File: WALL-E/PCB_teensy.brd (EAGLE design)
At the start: 92.8 x 115.8 mm, 42 parts, among them U4 R-78E5.0-0.5

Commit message: cleaned up each layer
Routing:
- net 8: track 90.0 -> 90.5 mm
- net 0/RX: track 94.4 -> 93.9 mm
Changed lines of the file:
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@@
 <contactref element="U$1" pad="0/RX"/>
 <contactref element="J1" pad="3"/>
-<wire x1="62.9" y1="29.37" x2="62.9" y2="28.85" width="0.1524" layer="1"/>
 <via x="69.5" y="30.25" extent="1-16" drill="0.35"/>
 <wire x1="74.98" y1="102.48" x2="86.75" y2="102.48" width="0.1524" layer="1"/>
@@
 <via x="69.5" y="27.75" extent="1-16" drill="0.35"/>
 <wire x1="50.2" y1="29.37" x2="52.8075" y2="26.7625" width="0.1524" layer="1"/>
-<wire x1="52.8075" y1="26.7625" x2="52.8075" y2="25.80045625" width="0.1524" layer="1"/>
-<wire x1="52.8075" y1="25.80045625" x2="53.85795625" y2="24.75" width="0.1524" layer="1"/>
-<wire x1="53.85795625" y1="24.75" x2="59.5" y2="24.75" width="0.1524" layer="1"/>
-<wire x1="59.5" y1="24.75" x2="62.4452" y2="27.6952" width="0.1524" layer="1"/>
-<wire x1="69.4452" y1="27.6952" x2="69.5" y2="27.75" width="0.1524" layer="1"/>
-<wire x1="62.4452" y1="27.6952" x2="69.4452" y2="27.6952" width="0.1524" layer="1"/>
+<wire x1="52.8075" y1="25.80045625" x2="52.8075" y2="26.7625" width="0.1524" layer="1"/>
+<wire x1="59.5" y1="25" x2="62.9452" y2="27.4452" width="0.1524" layer="1"/>
 <wire x1="69.5" y1="27.75" x2="73.25" y2="31.5" width="0.1524" layer="15"/>
 <wire x1="73.25" y1="31.5" x2="73.25" y2="84.25" width="0.1524" layer="15"/>
@@
 <wire x1="73.25" y1="84.25" x2="77.48" y2="88.48" width="0.1524" layer="1"/>
 <wire x1="77.48" y1="88.48" x2="86.75" y2="88.48" width="0.1524" layer="1"/>
+<wire x1="53.60795625" y1="25" x2="52.8075" y2="25.80045625" width="0.1524" layer="1"/>
+<wire x1="59.5" y1="25" x2="53.60795625" y2="25" width="0.1524" layer="1"/>
+<wire x1="69.1952" y1="27.4452" x2="69.5" y2="27.75" width="0.1524" layer="1"/>
+<wire x1="62.9452" y1="27.4452" x2="69.1952" y2="27.4452" width="0.1524" layer="1"/>
 </signal>
 <signal name="6">
@@
 <via x="68.5" y="26.5" extent="1-16" drill="0.35"/>
 <wire x1="50.25" y1="25.75" x2="51.5548" y2="24.4452" width="0.1524" layer="1"/>
-<wire x1="61.68105625" y1="26.5" x2="68.5" y2="26.5" width="0.1524" layer="1"/>
-<wire x1="59.62625625" y1="24.4452" x2="61.68105625" y2="26.5" width="0.1524" layer="1"/>
+<wire x1="62.68105625" y1="26.5" x2="68.5" y2="26.5" width="0.1524" layer="1"/>
+<wire x1="59.62625625" y1="24.4452" x2="62.68105625" y2="26.5" width="0.1524" layer="1"/>
 <wire x1="51.5548" y1="24.4452" x2="59.62625625" y2="24.4452" width="0.1524" layer="1"/>
 <wire x1="68.5" y1="26.5" x2="69.75" y2="26.5" width="0.1524" layer="15"/>
@@
 <wire x1="45.12" y1="29.37" x2="47.5" y2="26.99" width="0.1524" layer="1"/>
 <wire x1="47.5" y1="26.99" x2="47.5" y2="25.5" width="0.1524" layer="1"/>
-<wire x1="47.5" y1="25.5" x2="48.8596" y2="24.1404" width="0.1524" layer="1"/>
-<wire x1="48.8596" y1="24.1404" x2="59.7525125" y2="24.1404" width="0.1524" layer="1"/>
-<wire x1="59.7525125" y1="24.1404" x2="60.80605625" y2="25.19394375" width="0.1524" layer="1"/>
-<wire x1="60.80605625" y1="25.19394375" x2="69.44394375" y2="25.19394375" width="0.1524" layer="1"/>
+<wire x1="47.5" y1="25.5" x2="48.8596" y2="23.8904" width="0.1524" layer="1"/>
+<wire x1="48.8596" y1="23.8904" x2="59.7525125" y2="23.8904" width="0.1524" layer="1"/>
+<wire x1="59.7525125" y1="23.8904" x2="61.80605625" y2="25.19394375" width="0.1524" layer="1"/>
+<wire x1="61.80605625" y1="25.19394375" x2="69.44394375" y2="25.19394375" width="0.1524" layer="1"/>
 <wire x1="69.44394375" y1="25.19394375" x2="69.5" y2="25.25" width="0.1524" layer="1"/>
 <via x="69.5" y="25.25" extent="1-16" drill="0.35"/>
@@
 <contactref element="J3" pad="4"/>
 <via x="68.5" y="24" extent="1-16" drill="0.35"/>
-<wire x1="59.87876875" y1="23.8356" x2="60.04316875" y2="24" width="0.1524" layer="1"/>
-<wire x1="60.04316875" y1="24" x2="68.5" y2="24" width="0.1524" layer="1"/>
-<wire x1="42.58" y1="29.37" x2="48.1144" y2="23.8356" width="0.1524" layer="1"/>
-<wire x1="48.1144" y1="23.8356" x2="59.87876875" y2="23.8356" width="0.1524" layer="1"/>
+<wire x1="48.1144" y1="23.3356" x2="42.58" y2="29.37" width="0.1524" layer="1"/>
 <wire x1="68.5" y1="24" x2="70" y2="24" width="0.1524" layer="15"/>
 <wire x1="70" y1="24" x2="76.25" y2="30.25" width="0.1524" layer="15"/>
@@
 <wire x1="76.25" y1="70.5" x2="77.69" y2="71.94" width="0.1524" layer="1"/>
 <wire x1="77.69" y1="71.94" x2="86.75" y2="71.94" width="0.1524" layer="1"/>
+<wire x1="68.5" y1="24" x2="67.8356" y2="23.3356" width="0.1524" layer="1"/>
+<wire x1="67.8356" y1="23.3356" x2="48.1144" y2="23.3356" width="0.1524" layer="1"/>
 </signal>
 <signal name="24">
@@
 <via x="66.75" y="37" extent="1-16" drill="0.35"/>
 <wire x1="66.75" y1="37" x2="76.75" y2="37" width="0.1524" layer="2"/>
-<wire x1="76.75" y1="37" x2="77" y2="37" width="0.1524" layer="2"/>
 <via x="81.75" y="26.25" extent="1-16" drill="0.35"/>
 <wire x1="81.75" y1="26.25" x2="81.77" y2="26.23" width="0.1524" layer="1"/>
@@
 <wire x1="21.53" y1="9.72" x2="21.53" y2="8.75" width="0.1524" layer="1"/>
 <wire x1="18.12" y1="13.13" x2="21.53" y2="9.72" width="0.1524" layer="1"/>
-<wire x1="21.53" y1="8.75" x2="26.03" y2="4.5" width="0.1524" layer="1"/>
-<wire x1="26.03" y1="4.5" x2="74.75" y2="4.5" width="0.1524" layer="1"/>
+<wire x1="21.53" y1="8.75" x2="25.78" y2="4.5" width="0.1524" layer="1"/>
+<wire x1="25.78" y1="4.5" x2="74.75" y2="4.5" width="0.1524" layer="1"/>
 <wire x1="74.75" y1="4.5" x2="77" y2="7" width="0.1524" layer="1"/>
 <wire x1="77" y1="7" x2="77" y2="39.5" width="0.1524" layer="1"/>
@@
 <wire x1="24.07" y1="9.68" x2="24.07" y2="8.75" width="0.1524" layer="1"/>
 <wire x1="20.62" y1="13.13" x2="24.07" y2="9.68" width="0.1524" layer="1"/>
-<wire x1="24.07" y1="8.75" x2="28.07" y2="5" width="0.1524" layer="1"/>
-<wire x1="28.07" y1="5" x2="74.25" y2="5" width="0.1524" layer="1"/>
+<wire x1="24.07" y1="8.75" x2="27.82" y2="5" width="0.1524" layer="1"/>
+<wire x1="27.82" y1="5" x2="74.25" y2="5" width="0.1524" layer="1"/>
 <wire x1="74.25" y1="5" x2="75.75" y2="6.5" width="0.1524" layer="1"/>
 <wire x1="75.75" y1="6.5" x2="75.75" y2="39.5" width="0.1524" layer="1"/>

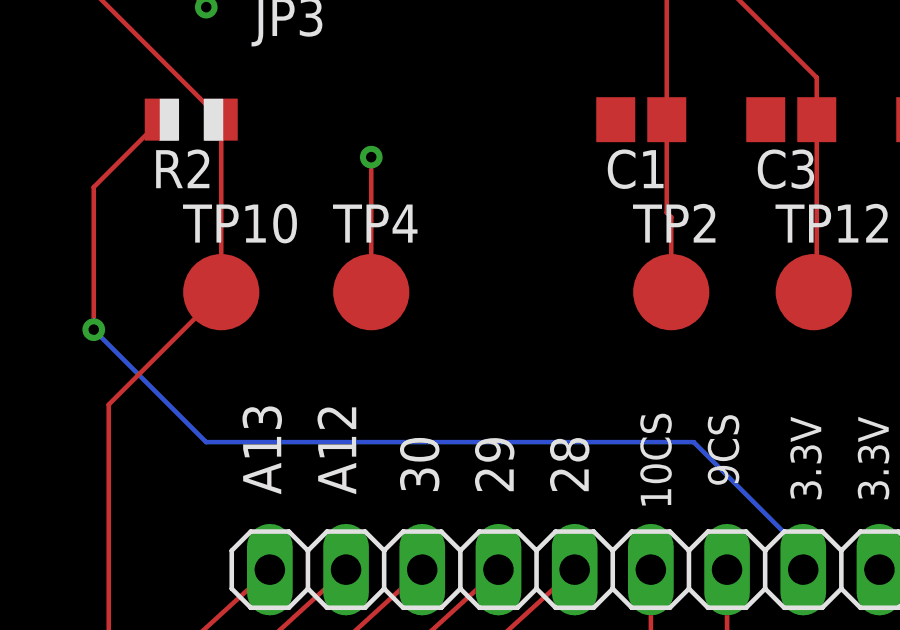
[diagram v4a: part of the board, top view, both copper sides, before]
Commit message: added tp1 for 3.3V
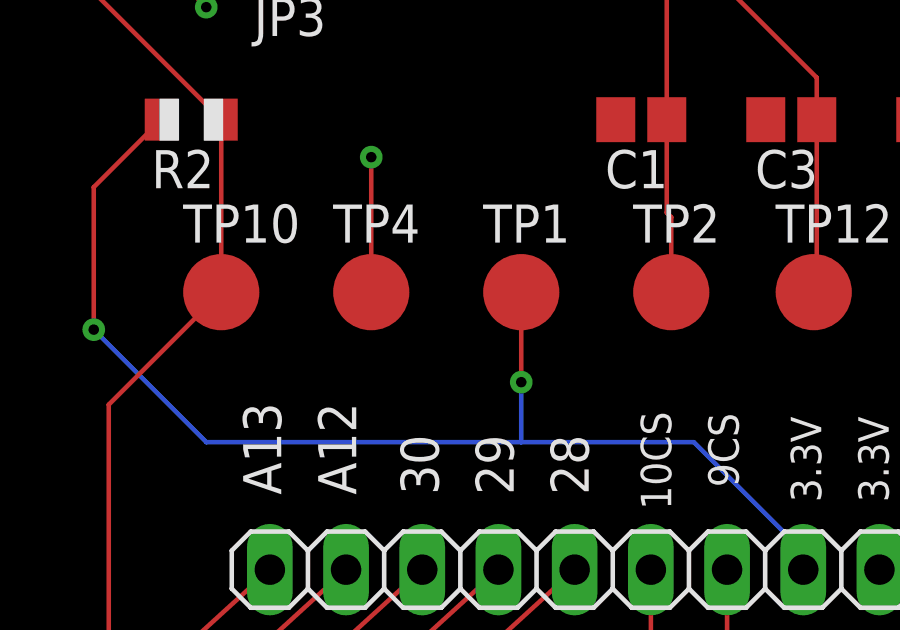
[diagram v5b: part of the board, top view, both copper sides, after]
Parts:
- added TP1: PTR1B2,54, testpad:B2,54
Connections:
- net 3.3V: now also TP1.TP
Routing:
- net 3.3V: track 100.1 -> 105.1 mm, vias 7 -> 8
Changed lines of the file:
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@@
 <element name="R7" library="adafruit" library_urn="urn:adsk.eagle:library:420" package="R0805" value="" x="39.25" y="62.5"/>
 <element name="R8" library="adafruit" library_urn="urn:adsk.eagle:library:420" package="R0805" value="" x="34.25" y="62.5"/>
+<element name="TP1" library="testpad" library_urn="urn:adsk.eagle:library:385" package="B2,54" package3d_urn="urn:adsk.eagle:package:27948/1" value="PTR1B2,54" x="18.25" y="45.5">
+<attribute name="TP_SIGNAL_NAME" value="" x="18.25" y="45.5" size="1.778" layer="27" display="off"/>
+</element>
 </elements>
 <signals>
@@
 <via x="4" y="44.25" extent="1-16" drill="0.35"/>
 <wire x1="4" y1="44.25" x2="7.75" y2="40.5" width="0.1524" layer="16"/>
-<wire x1="7.75" y1="40.5" x2="24" y2="40.5" width="0.1524" layer="16"/>
+<wire x1="7.75" y1="40.5" x2="18.25" y2="40.5" width="0.1524" layer="16"/>
+<wire x1="18.25" y1="40.5" x2="24" y2="40.5" width="0.1524" layer="16"/>
 <wire x1="24" y1="40.5" x2="27.65" y2="36.85" width="0.1524" layer="16"/>
 <wire x1="27.65" y1="36.85" x2="27.65" y2="36.25" width="0.1524" layer="16"/>
@@
 <wire x1="53.25" y1="66" x2="53.25" y2="62.5" width="0.1524" layer="1"/>
 <wire x1="58.25" y1="66" x2="58.25" y2="62.5" width="0.1524" layer="1"/>
+<contactref element="TP1" pad="TP"/>
+<wire x1="18.25" y1="45.5" x2="18.25" y2="42.5" width="0.1524" layer="1"/>
+<via x="18.25" y="42.5" extent="1-16" drill="0.35"/>
+<wire x1="18.25" y1="42.5" x2="18.25" y2="40.5" width="0.1524" layer="16"/>
 </signal>
 <signal name="0/RX">

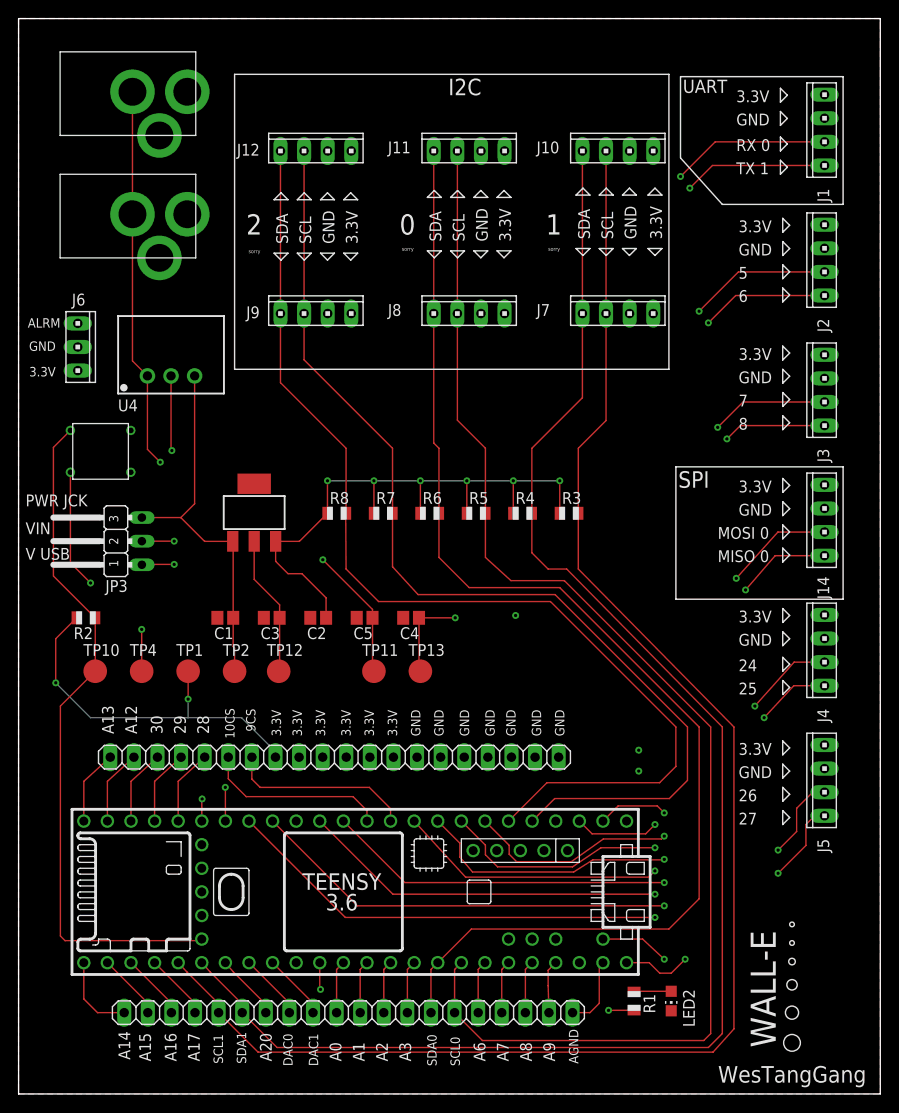
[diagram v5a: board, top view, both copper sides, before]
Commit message: combined top and bottom layers into one top layer. Also added power and ground to middle planes
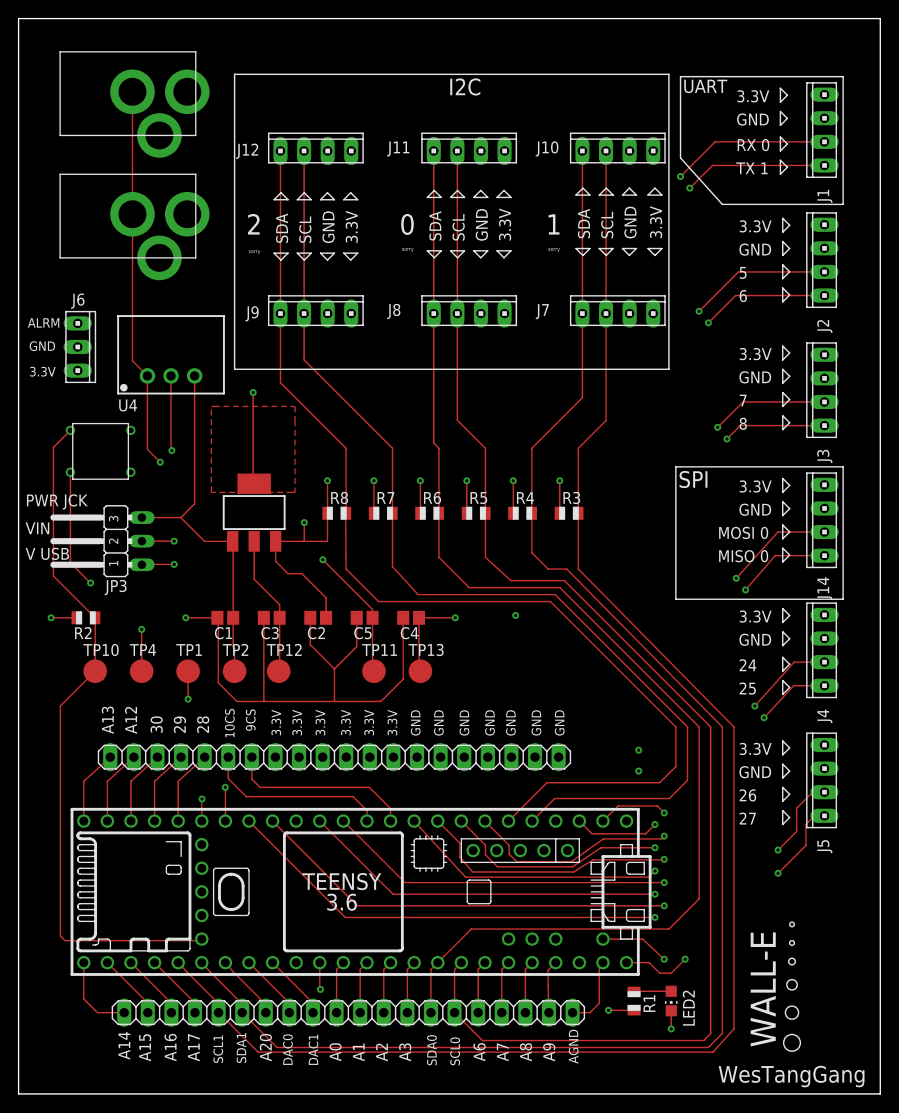
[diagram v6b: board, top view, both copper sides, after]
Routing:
- net GND: track 0.00 -> 76.2 mm, vias 0 -> 3
- net 3.3V: track 105.1 -> 49.4 mm, vias 8 -> 9
- added copper zone on layer 2, net GND
- added copper zone on layer 1, net N$6
- removed copper zone on layer 1, net GND

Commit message: moved light blue layer and light red  layer into one light red  layer
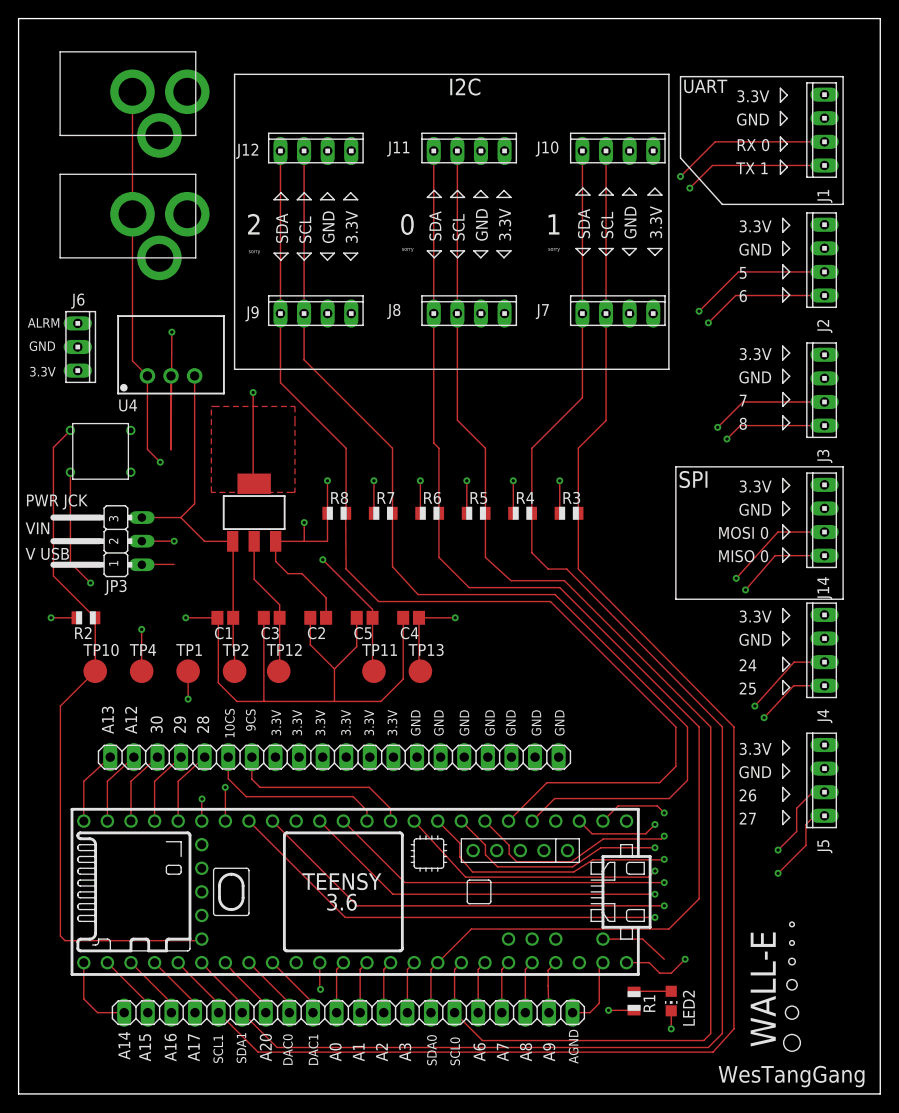
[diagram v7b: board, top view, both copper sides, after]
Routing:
- net 26: track 81.8 -> 152.7 mm, vias 3 -> 2
- net 27: track 82.7 -> 136.6 mm, vias 3 -> 2
- net N$1: track 60.1 -> 89.0 mm
- net N$5: track 53.1 -> 75.7 mm
- net ALARMPIN: track 97.8 -> 102.5 mm, vias 1 -> 0
- net N$2: track 95.4 -> 97.5 mm, vias 2 -> 0
- net VIN: track 98.9 -> 97.8 mm

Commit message: moved light red layer to bottom layer. Routing should be done
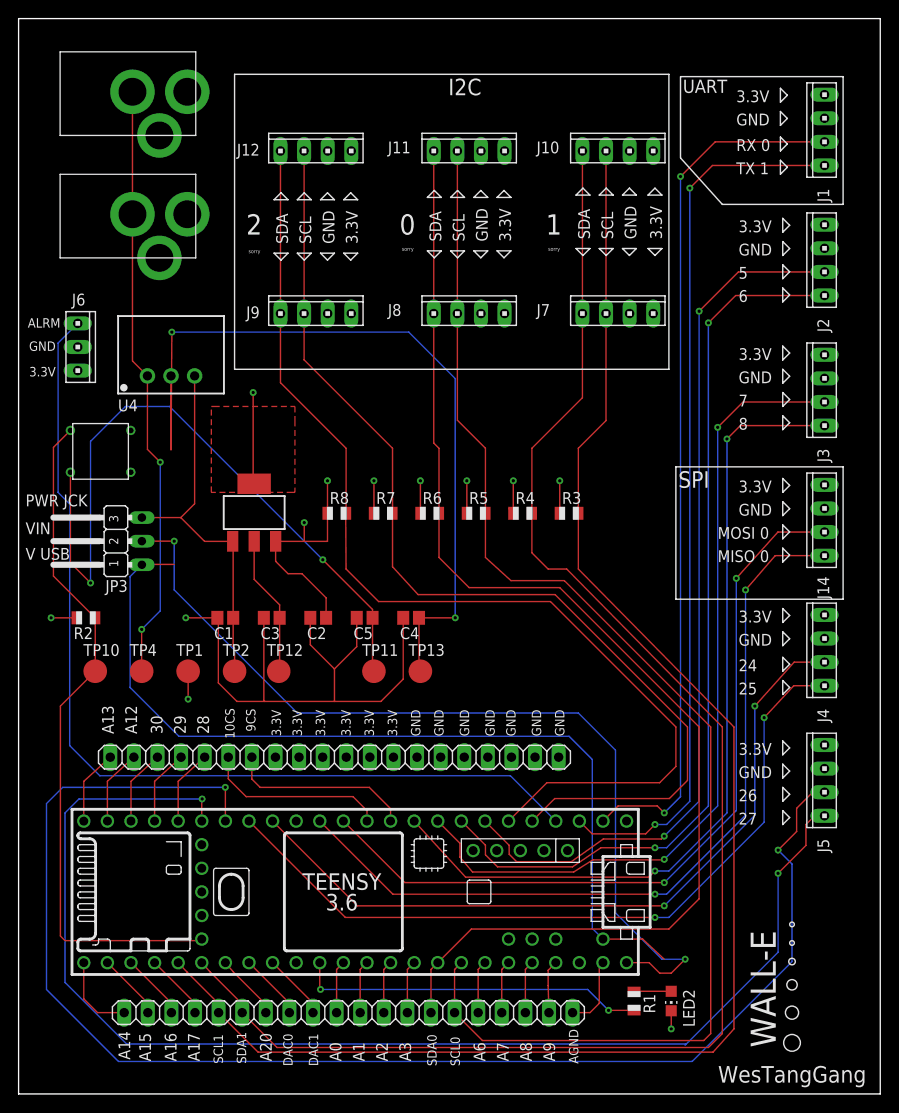
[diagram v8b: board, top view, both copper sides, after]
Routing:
- net 26: track 152.7 -> 153.5 mm
- net 27: track 136.6 -> 137.2 mm
- added copper zone on layer 1, net GND
- removed copper zone on layer 1, net N$6
